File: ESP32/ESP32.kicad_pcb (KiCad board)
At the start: 2 copper layers, 4 parts

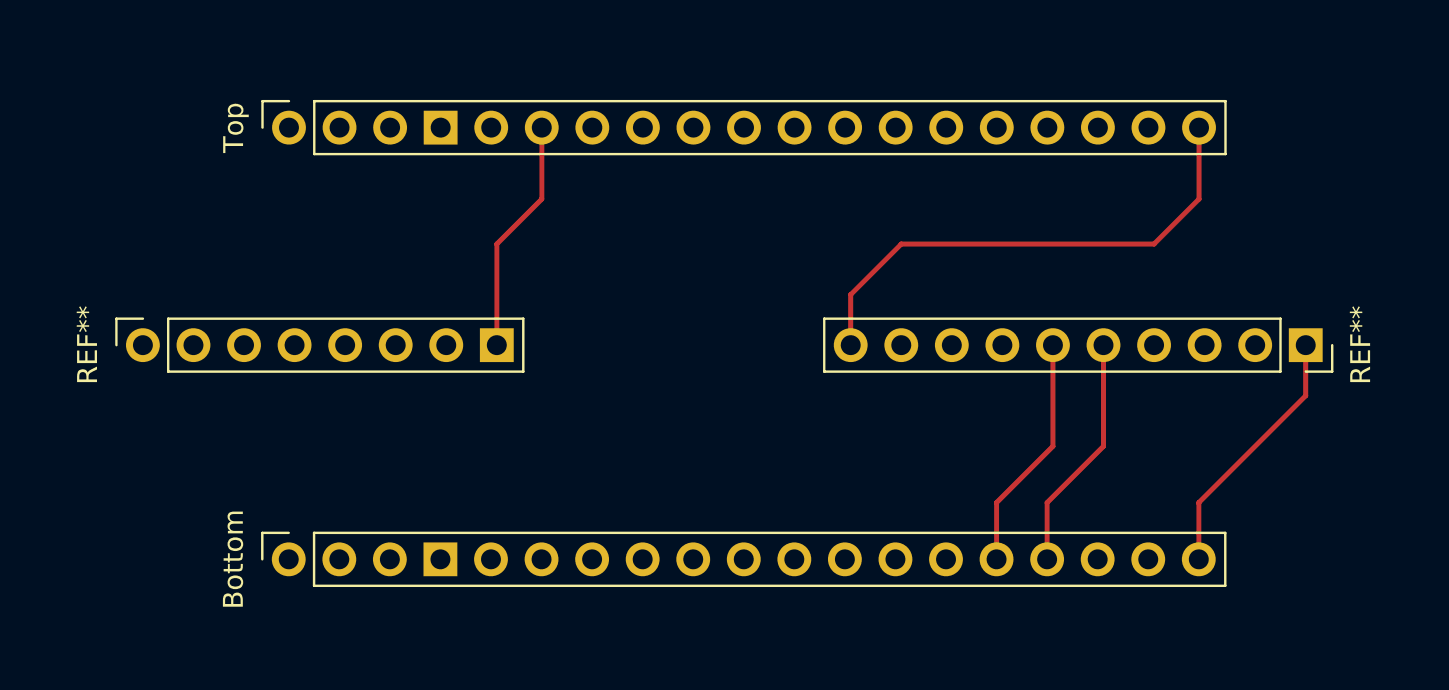
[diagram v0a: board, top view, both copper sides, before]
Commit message: Added border and measurements
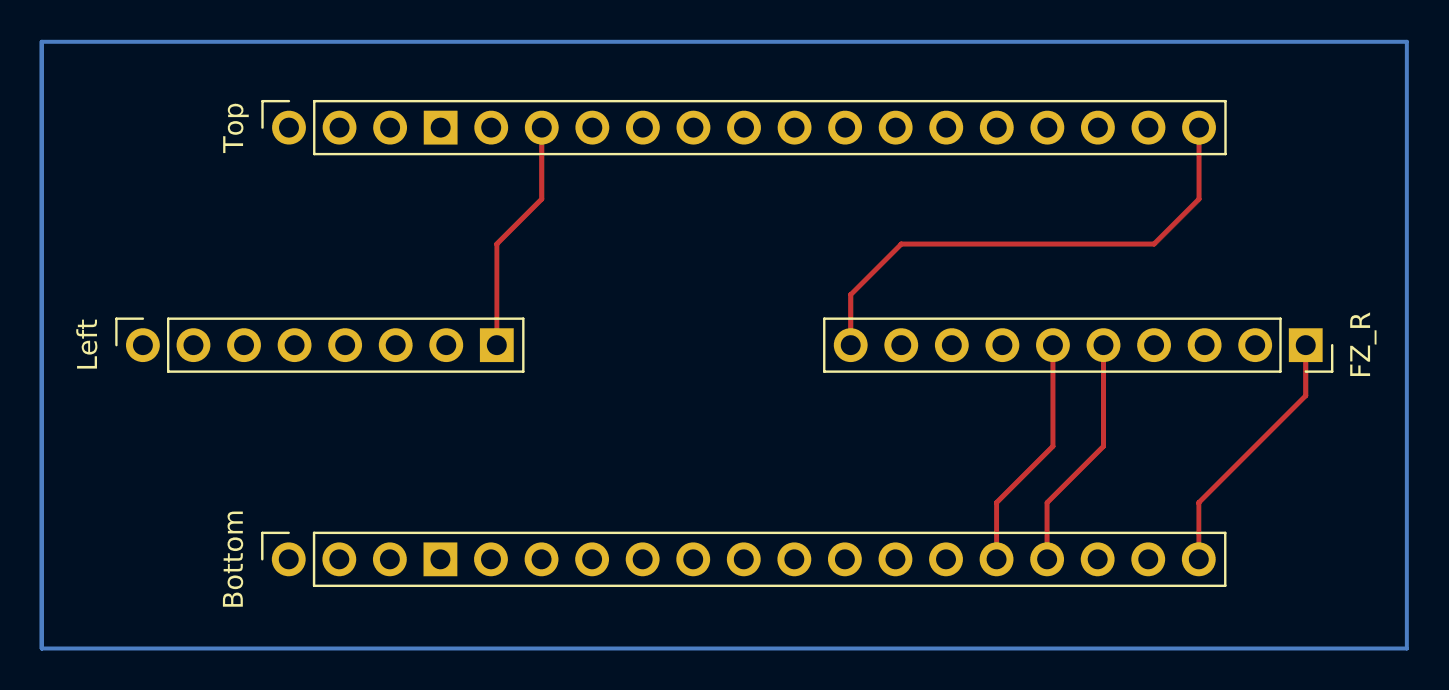
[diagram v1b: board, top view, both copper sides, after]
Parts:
- Bottom: value ESP32 Bottom -> ESP_B
- Left: renamed from REF**; value Left -> FZ_L
- Top: value ESP32 Top -> ESP_T
- renumbered REF** to FZ_R
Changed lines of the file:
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@@
     (tags "Through hole socket strip THT 1x10 2.54mm single row")
     (attr through_hole)
-    (fp_text reference "REF**" (at 0 -2.77 90) (layer "F.SilkS")
+    (fp_text reference "FZ_R" (at 0 -2.77 90) (layer "F.SilkS")
         (effects (font (size 1 1) (thickness 0.15)))
     )
@@
     (tags "Through hole socket strip THT 1x08 2.54mm single row")
     (attr through_hole)
-    (fp_text reference "REF**" (at 0 -2.77 90) (layer "F.SilkS")
-        (effects (font (size 1 1) (thickness 0.15)))
-    )
-    (fp_text value "Left" (at 0 20.55 90) (layer "F.Fab")
+    (fp_text reference "Left" (at 0 -2.77 90) (layer "F.SilkS")
+        (effects (font (size 1 1) (thickness 0.15)))
+    )
+    (fp_text value "FZ_L" (at 0 20.55 90) (layer "F.Fab")
         (effects (font (size 1 1) (thickness 0.15)))
     )
@@
         (effects (font (size 1 1) (thickness 0.15)))
     )
-    (fp_text value "ESP32 Bottom" (at 0 48.49 90) (layer "F.Fab")
+    (fp_text value "ESP_B" (at 0 48.49 90) (layer "F.Fab")
         (effects (font (size 1 1) (thickness 0.15)))
     )
@@
         (effects (font (size 1 1) (thickness 0.15)))
     )
-    (fp_text value "ESP32 Top" (at 0 48.49 90) (layer "F.Fab")
+    (fp_text value "ESP_T" (at 0 48.49 90) (layer "F.Fab")
         (effects (font (size 1 1) (thickness 0.15)))
     )
@@
     )
   )
+  (gr_rect (start 104.14 48.26) (end 172.72 78.74)
+    (stroke (width 0.2) (type default)) (fill none) (layer "B.Cu"))
+  (gr_rect (start 104.14 48.26) (end 104.14 78.74)
+    (stroke (width 0.2) (type default)) (fill none) (layer "B.Cu"))
   (dimension (type aligned) (layer "F.Cu")
     (pts (xy 127 68.58) (xy 144.78 68.58))
@@
   )
   (dimension (type aligned) (layer "F.Cu")
-    (pts (xy 175.26 50.8) (xy 175.26 76.2))
-    (height 0)
-    (gr_text "25.4000 mm" (at 173.46 63.5 90) (layer "F.Cu")
-      (effects (font (size 1.5 1.5) (thickness 0.3)))
-    )
-    (format (prefix "") (suffix "") (units 3) (units_format 1) (precision 4))
-    (style (thickness 0.2) (arrow_length 1.27) (text_position_mode 0) (extension_height 0.58642) (extension_offset 0.5) keep_text_aligned)
+    (pts (xy 177.8 50.8) (xy 177.8 76.2))
+    (height 0)
+    (gr_text "25.4000 mm" (at 177.8 63.5 90) (layer "F.Cu")
+      (effects (font (size 1.5 1.5) (thickness 0.3)))
+    )
+    (format (prefix "") (suffix "") (units 3) (units_format 1) (precision 4))
+    (style (thickness 0.2) (arrow_length 1.27) (text_position_mode 2) (extension_height 0.58642) (extension_offset 0.5) keep_text_aligned)
+  )
+  (dimension (type aligned) (layer "B.Cu")
+    (pts (xy 101.6 78.74) (xy 101.6 48.26))
+    (height 0)
+    (gr_text "30.4800 mm" (at 101.6 63.5 90) (layer "B.Cu")
+      (effects (font (size 1.5 1.5) (thickness 0.3)))
+    )
+    (format (prefix "") (suffix "") (units 3) (units_format 1) (precision 4))
+    (style (thickness 0.2) (arrow_length 1.27) (text_position_mode 2) (extension_height 0.58642) (extension_offset 0.5) keep_text_aligned)
+  )
+  (dimension (type aligned) (layer "B.Cu")
+    (pts (xy 104.14 81.28) (xy 172.72 81.28))
+    (height 0)
+    (gr_text "68.5800 mm" (at 138.43 81.28) (layer "B.Cu")
+      (effects (font (size 1.5 1.5) (thickness 0.3)))
+    )
+    (format (prefix "") (suffix "") (units 3) (units_format 1) (precision 4))
+    (style (thickness 0.2) (arrow_length 1.27) (text_position_mode 2) (extension_height 0.58642) (extension_offset 0.5) keep_text_aligned)
   )
   (segment (start 154.647072 74.260554) (end 154.647072 71.412928) (width 0.25) (layer "F.Cu") (net 0))

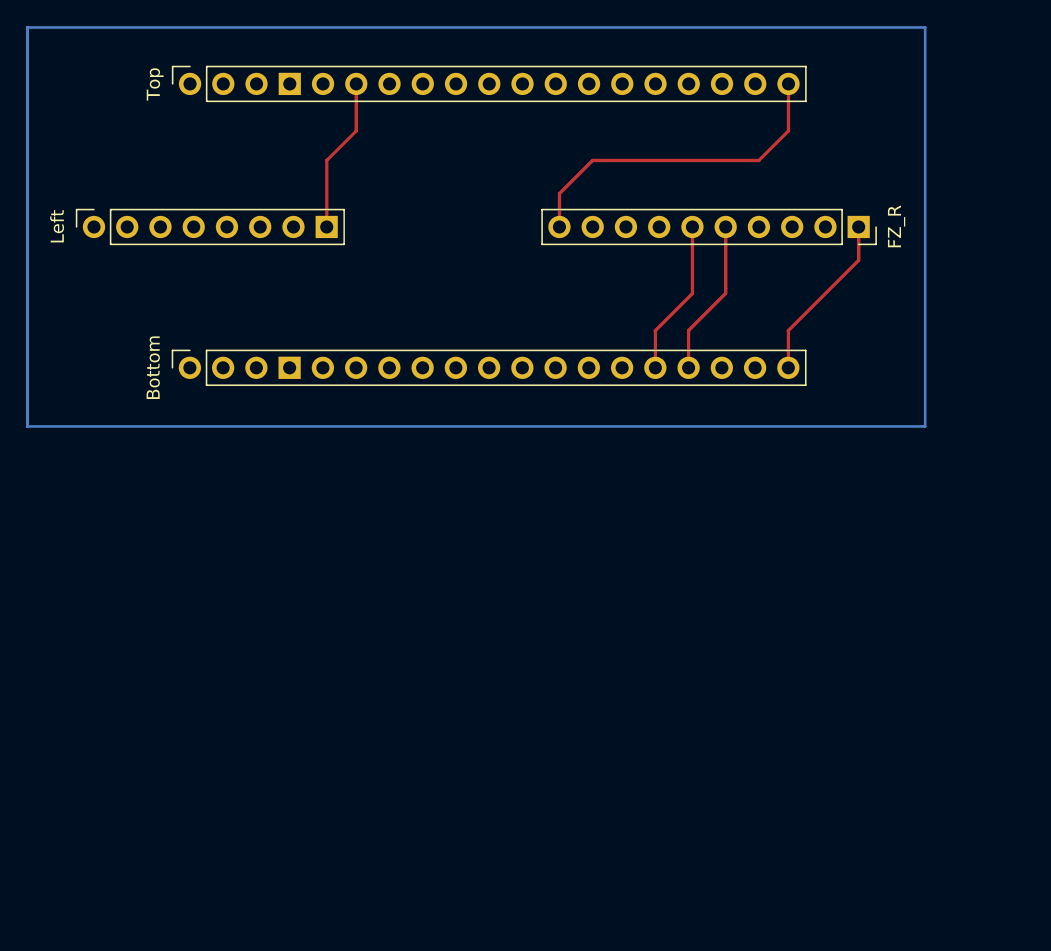
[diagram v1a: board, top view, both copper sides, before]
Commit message: Fixed spacing
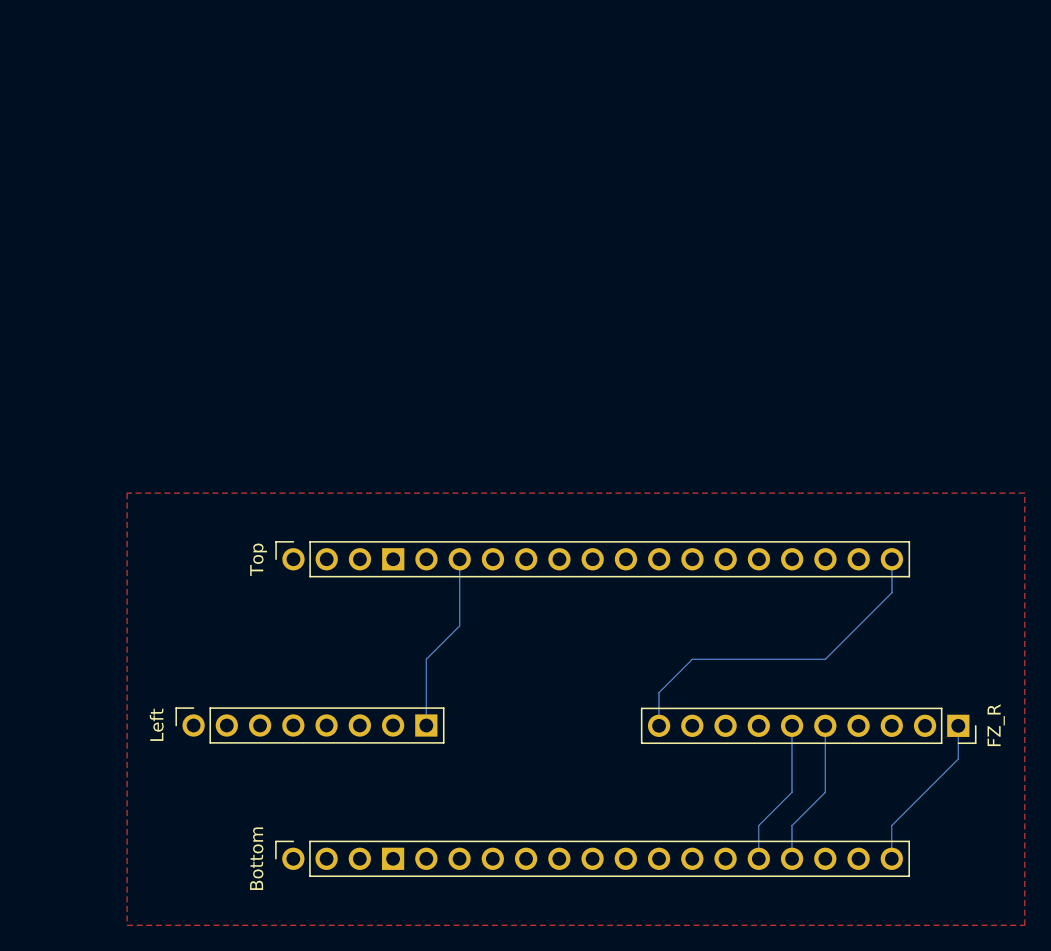
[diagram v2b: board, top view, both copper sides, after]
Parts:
- moved FZ_R 38.9 mm to (175.2, 101.6)
- moved Left 38.8 mm to (116.8, 101.6)
- moved Bottom 38.3 mm to (124.5, 111.8)
- moved Top 37.2 mm to (124.5, 88.9)
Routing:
- added copper zone on F.Cu, net (none)
